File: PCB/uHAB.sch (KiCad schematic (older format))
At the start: 0 parts

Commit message: Finished power system design, added some custom schematic symbols, updated component selection document
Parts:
- added C? (x5): 47uF, symbol C
- added C?: 0.1uF, symbol C
- added D?: LED, symbol LED
- added F?: 0ZCJ0025AF2E, symbol Polyfuse
- added J?: Programming, symbol USB_OTG
- added J?: Battery_Input (5.6V-18V), symbol Conn_01x02
- added J?: Remove_Before_Flight_(RBF), symbol Conn_01x02
- added J?: Helmet_RBF_Jumper, symbol Conn_01x03
- added Q? (x3): SSM3J358R,LF, symbol Q_PMOS_GSD
- added Q?: NTR4003NTD, symbol Q_NMOS_GSD
- added R? (x2): 100k, symbol R
- added R?: R, symbol R
- added R? (x3): 10k, symbol R
- added R? (x2): 22, symbol R
- added U?: LDL1117S50R, TO_SOT_Packages_SMD:SOT-223-3Lead_TabPin2, symbol AP1117-15
- added U?: LDL1117S33R, TO_SOT_Packages_SMD:SOT-223-3Lead_TabPin2, symbol AP1117-15
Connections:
- new net: F?.2, J?.1 (VBUS)
- new net: J?.2 (D-), R?.2
- new net: J?.3 (D+), R?.2
- new net: J?.2 (Pin_2), Q?.3 (D)
- new net: C?.1, Q?.2 (S), Q?.2 (S), R?.1
- new net: Q?.1 (G), R?.1
- new net: D?.2 (A), R?.1
- new net: D?.1 (K), Q?.3 (D)
- new net: Q?.1 (G), R?.1, R?.1
- new net: J?.1 (Pin_1), Q?.1 (G), R?.2
- new net +3.3V: C?.1, Q?.1 (G), R?.2, U?.2 (VO)
- new net +5V: C?.1, C?.1, Q?.3 (D), R?.2, U?.2 (VO), U?.3 (VI)
- new net GND: C?.2, C?.2, C?.2, C?.2, C?.2, C?.2, J?.1 (Pin_1), J?.3 (Pin_3), J?.5 (GND), J?.6 (Shield), Q?.2 (S), R?.1, R?.2, R?.2, U?.1 (GND), U?.1 (GND)
- new net HELMET_RBF: J?.1 (Pin_1)
- new net MAIN_POWER: C?.1, Q?.3 (D), R?.2, U?.3 (VI)
- new net UHAB_RBF: J?.2 (Pin_2), J?.2 (Pin_2)
- new net USB_D+: R?.1
- new net USB_D-: R?.1
- new net USB_POWER: C?.1, F?.1, Q?.2 (S)
- no-connect marks 0 -> 1
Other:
- note added: "Connector PN: \n5-103635-1\n\nMate PN: \n104257-1\n\nTerminal PN: \n1-104480-7\n----------"
- note added: "Connector PN: \nDF22R-2P-7.92DS(05)\n\nMate PN: \nDF22R-2S-7.92C(28)\n\nTerminal PN: \nDF22-1416SCF"
- note added: "Connector PN: \nUJ2-MIBH-4-SMT-TR"
- note added: "Header PN: \nM20-9990346\n\nJumper PN:\nSTC02SYAN"
- note added: "If main power is present, the USB power will\nbe blocked. If main power is not present, the\nUSB power will supply the 5V (and 3.3V) rail."
- note added: "Linear Regulators"
- note added: "Note: Both 5V and 3.3V must be present to \nilluminate the power good indication LED"
- note added: "Power Status Indication LED"
- note added: "Recommended:\n-2S LiPo Battery Pack\n-2S 18650 Battery Pack\n-9V Battery\n----------------"
- note added: "Remove Before Flight"
- note added: "Reverse\nPolarity\nProtection"
- note added: "USB Power Behavior"

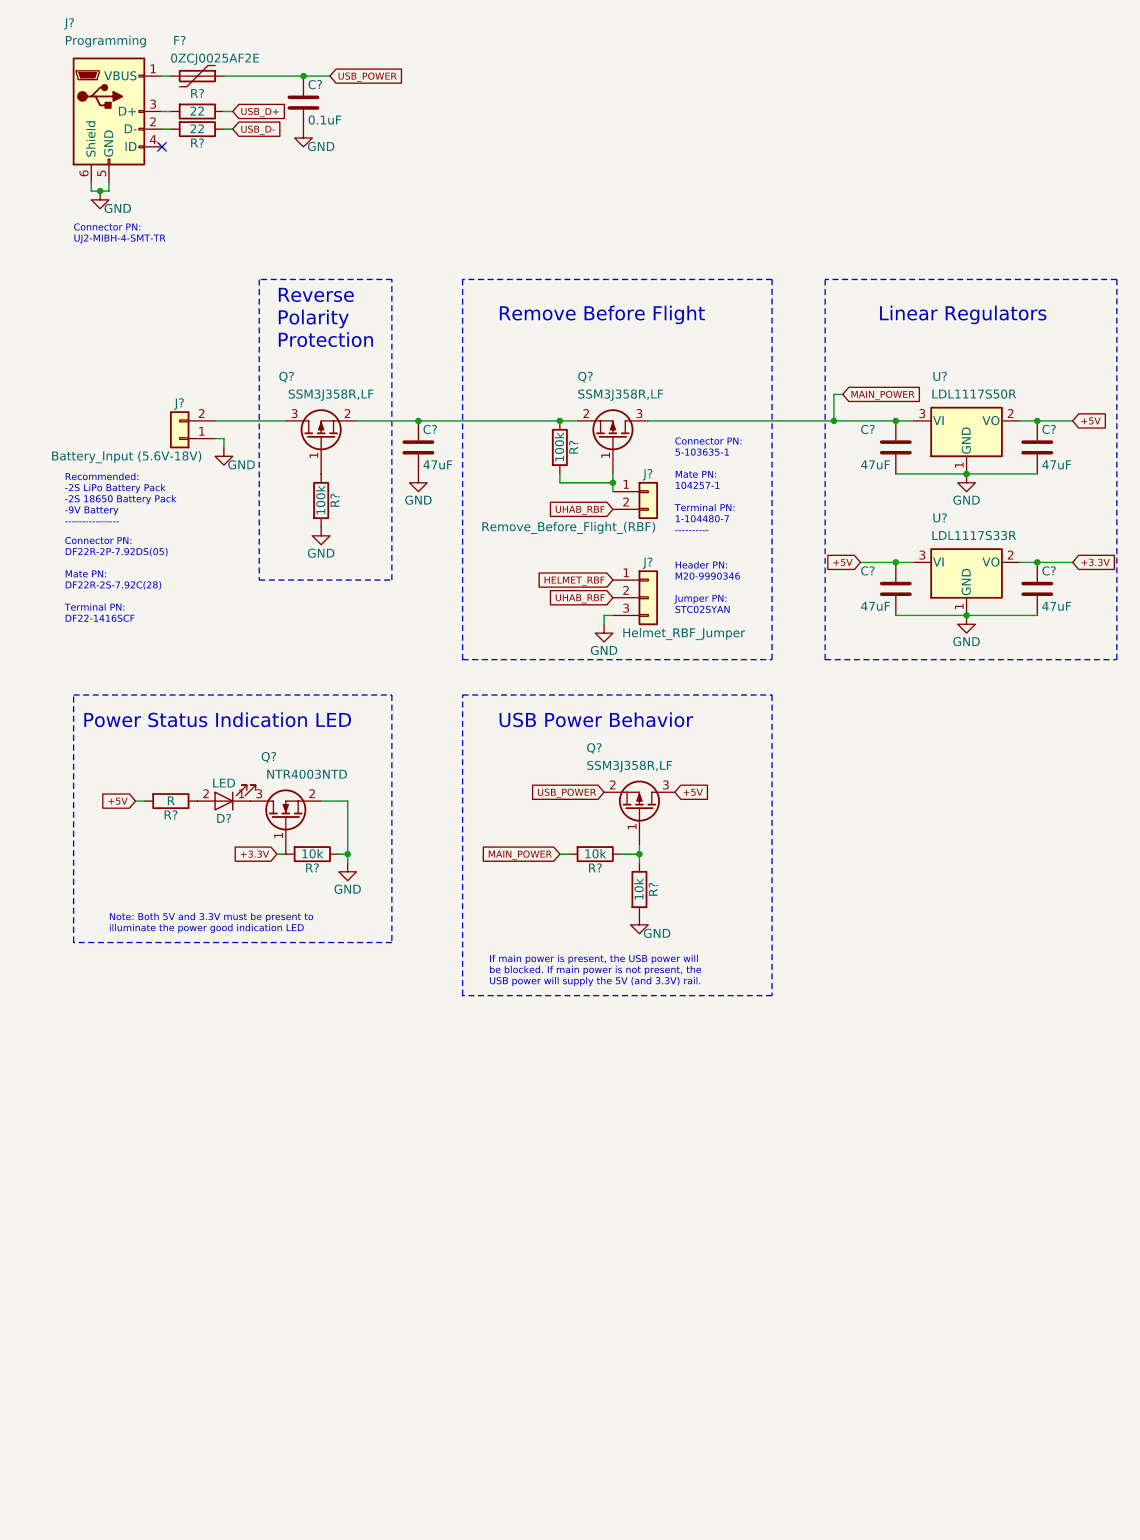
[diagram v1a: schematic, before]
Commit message: Added GPS Schematic, GPS datasheet, GPS user guide
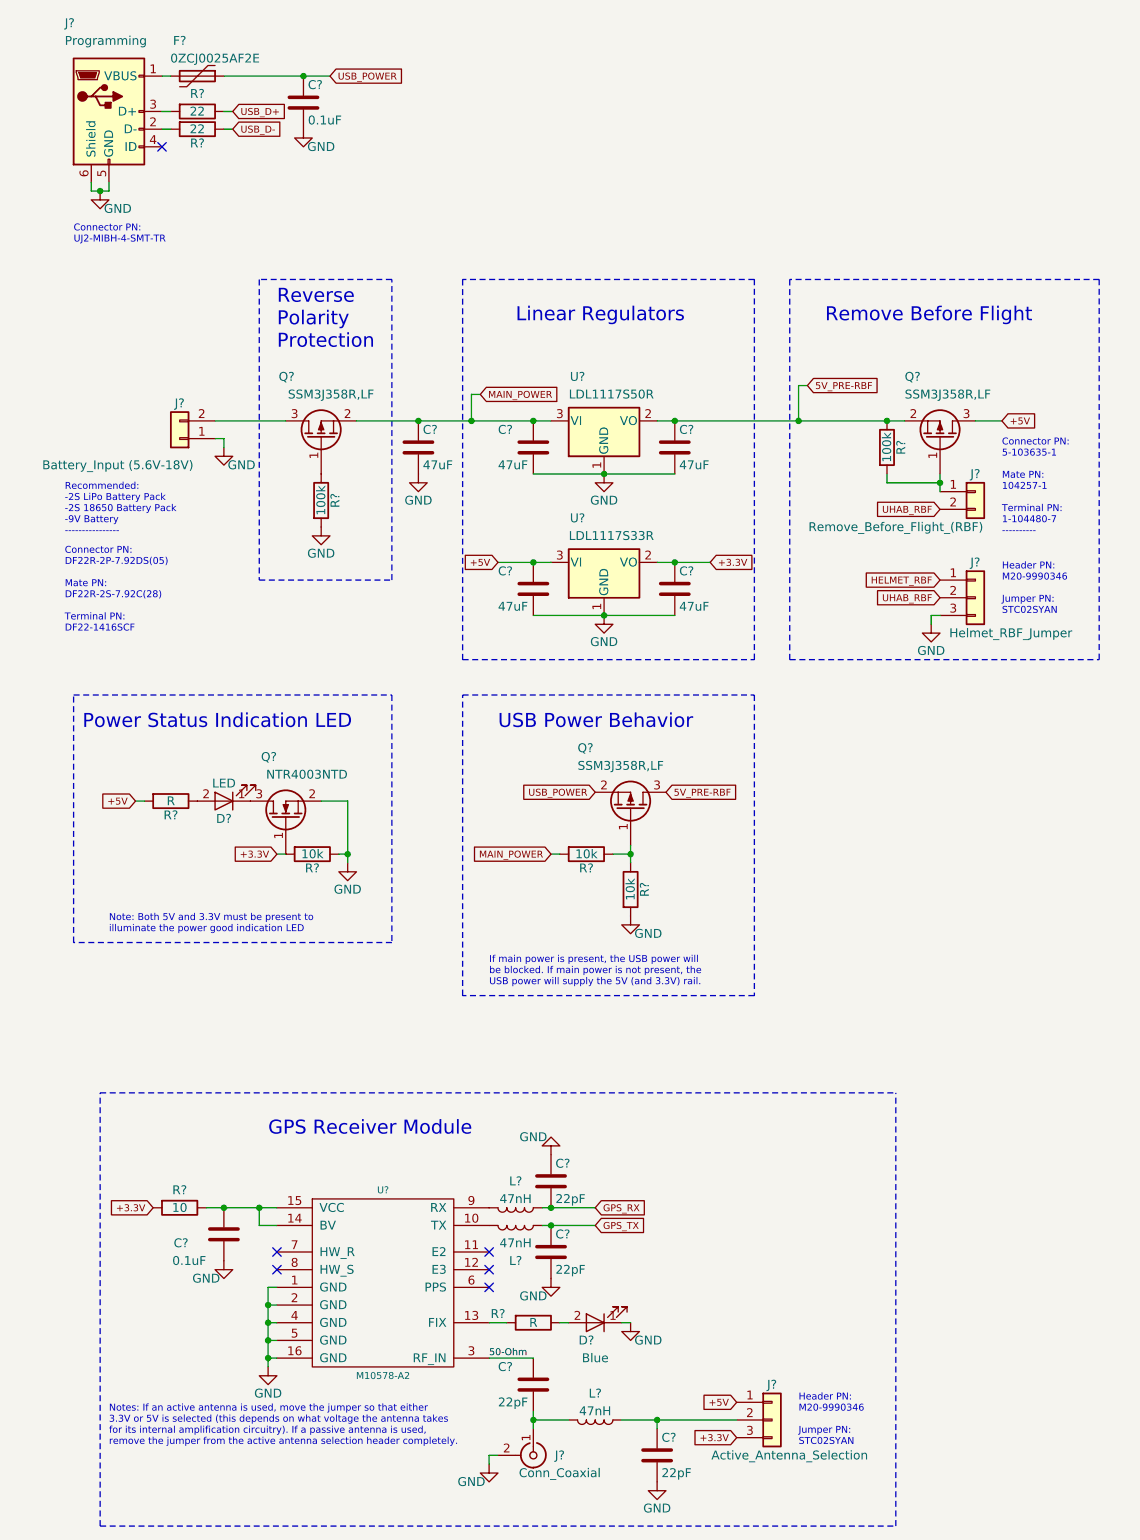
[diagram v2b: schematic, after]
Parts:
- added C?: 0.1uF, symbol C
- added C? (x4): 22pF, symbol C
- added D?: Blue, symbol LED
- added J?: Conn_Coaxial, symbol Conn_Coaxial
- added J?: Active_Antenna_Selection, symbol Conn_01x03
- added L? (x3): 47nH, symbol L
- added R?: 10, symbol R
- added R?: R, symbol R
- added U?: M10578-A2, symbol M10578-A2
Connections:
- net +3.3V: now also J?.3 (Pin_3), R?.2
- net +5V: now also Q?.3 (D), J?.1 (Pin_1); no longer C?.1, Q?.3 (D), U?.2 (VO)
- net GND: now also C?.1, C?.1, C?.2, C?.2, D?.1 (K), J?.2 (Ext), U?.1 (GND), U?.16 (GND), U?.2 (GND), U?.4 (GND), U?.5 (GND)
- net MAIN_POWER: now also C?.1, Q?.2 (S); no longer Q?.3 (D)
- net 5V_PRE-RBF: now reaches Q?.2 (S), R?.1
- net 5V_PRE-RBF: now also C?.1, Q?.3 (D), U?.2 (VO); no longer C?.1, Q?.2 (S)
- new net: L?.2, U?.10 (TX)
- new net: R?.2, U?.13 (FIX)
- new net: C?.2, R?.1, U?.14 (BV), U?.15 (VCC)
- new net: L?.2, U?.9 (RX)
- new net: D?.2 (A), R?.1
- new net: C?.2, J?.1 (In), L?.2
- new net: C?.1, J?.2 (Pin_2), L?.1
- new net 50-Ohm: C?.1, U?.3 (RF_IN)
- new net GPS_RX: C?.2, L?.1
- new net GPS_TX: C?.1, L?.1
- no-connect marks 1 -> 6
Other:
- note added: "GPS Receiver Module\n"
- note added: "Notes: If an active antenna is used, move the jumper so that either \n3.3V or 5V is selected (this depends on what voltage the antenna takes \nfor its internal amplification circuitry). If a passive antenna is used,\nremove the jumper from the active antenna selection header completely."
- moved on the sheet: C?, J?, Q?, R?, U?

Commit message: Added a ton to the schematic and included some additional documentation. Saving progress.
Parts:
- added C?: .01uF, symbol C
- added C?: 0.1uF, symbol C
- added C? (x16): 100nF, symbol C
- added C?: 10pF, symbol C
- added C? (x2): 10uF, symbol C
- added C? (x2): 12pF, symbol C
- added C?: 10nF, symbol C
- added C? (x2): 4.7pF, symbol C
- added D? (x3): LTST-C190KRKT, symbol LED
- added D?: 6.2V, symbol D_Zener
- added D?: LTST-C194KGKT, symbol LED
- added D?: LTST-C191TBKT, symbol LED
- added J?: Conn_Coaxial, symbol Conn_Coaxial
- added J?: Balloon_Cutdown, symbol Conn_01x02
- added J?: JTAG, symbol Conn_02x05_Odd_Even
- added L? (x3): BLM18PG471SN1, symbol L
- added Q?: SSM3J358R,LF, symbol Q_PMOS_GSD
- added Q? (x5): NTR4003NT1G, symbol Q_NMOS_GSD
- added Q?: IRLML62444, symbol Q_NMOS_GSD
- added R?: 0, symbol R
- added R? (x11): 100k, symbol R
- added R?: 680, symbol R
- added R?: 130, symbol R
- added R? (x2): 300, symbol R
- added R?: 170, symbol R
- added R? (x2): 10, symbol R
- added R?: 5.6k, symbol R
- added SW?: SW_Push, symbol SW_Push
- added U?: Radiometrix_HX1, symbol Radiometrix_HX1
- added U?: AT25DN256, symbol AT25DN256
- added U?: BLM18PG471SN1, MODULE, symbol ATSAMV71Q20B-AABT
- added Y?: 12MHz, symbol Crystal
- added Y?: 32.768kHz, symbol Crystal
- C?: value 0.1uF -> 47uF
- D?: value LED -> LTST-C194KGKT
- D?: value Blue -> LTST-C191TBKT
- Q?: value NTR4003NTD -> NTR4003NT1G
- R?: value R -> 300
- R? (x3): value 10k -> 100k
- R?: value R -> 170
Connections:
- net labels added: APRS_TX_5, BLUE_LED, CUTDOWN_ARM, CUTDOWN_FIRE, GREEN_LED, JTAGSEL, MEM_CS, MEM_MISO, MEM_MOSI, MEM_SCLK, PA00, PA01, PA02, PA03, PA04, PA05, PA06, PA09, PA10, PA11, PA12, PA13, PA14, PA15, PA16, PA17, PA18, PA19, PA20, PA21, PA22, PA23, PA24, PA25, PA26, PA27, PA28, PA29, PA30, PA31, PB00, PB01, PB02, PB03, PB04, PB05,TRACESWO, PB06,SWDIO, PB07,SWCLK, PB12, PB13, PC00, PC01, PC02, PC03, PC04, PC05, PC06, PC07, PC08, PC09, PC10, PC11, PC12, PC13, PC14, PC15, PC16, PC17, PC18, PC19, PC20, PC21, PC22, PC23, PC24, PC25, PC26, PC27, PC28, PC29, PC30, PC31, PD00, PD01, PD02, PD03, PD04, PD05, PD06, PD07, PD08, PD09, PD10, PD11, PD12, PD13, PD14, PD15, PD16, PD17, PD18, PD19, PD20, PD21, PD22, PD23, PD24, PD25, PD26, PD27, PD28, PD29, PD30, PD31, PE00, PE01, PE02, PE03, PE04, PE05, RED_LED, TARGET_RESET, TST, VDDCORE, VDDPLL, VDDUTMIC, XIN, XIN_32, XOUT, XOUT_32
- wire segments 57 -> 227
- no-connect marks 6 -> 10
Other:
- note added: "12MHz Crystal"
- note added: "256Kb Flash Memory"
- note added: "32.768kHz Crystal"
- note added: "APRS Transmit Radio"
- note added: "Balloon Cutdown"
- note added: "C_Crystal = 20pF\nmax ESR = 80 Ohm\nAccuracy = 20ppm"
- note added: "C_Crystal = 7pF\nmax ESR = 60 kOhm\nAccuracy = 20ppm"
- note added: "Controllable LEDs"
- note added: "Design Note: 10mA for this LED"
- note added: "External & Internal Power Decoupling"
- note added: "JTAG Programming Connector"
- note added: "Reset Pushbutton"
- note added: "USB Micro Power & Programming"
- moved on the sheet: C?, D?, F?, J?, L?, Q?, R?, U?

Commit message: Updated Schematic. Documentation still needs a lot of work
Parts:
- removed C?: .01uF, symbol C
- removed J?: Conn_Coaxial, symbol Conn_Coaxial
- removed R?: 0, symbol R
- removed U?: Radiometrix_HX1, symbol Radiometrix_HX1
- added .01uF: C, symbol C
- added C?: 100pF, symbol C
- added C?: 6.2pF, symbol C
- added C?: 12pF, symbol C
- added C? (x5): 560pF, symbol C
- added C?: 3.3pF, symbol C
- added C?: 22pF, symbol C
- added C?: 15pF, symbol C
- added C? (x2): 20pF, symbol C
- added C? (x3): 0.1uF, symbol C
- added D?: Green, symbol LED
- added D?: Red, symbol LED
- added L?: 200nH, symbol L
- added L?: 150nH, symbol L
- added L?: 470nH, symbol L
- added L?: 56nH, symbol L
- added L?: 82nH, symbol L
- added L?: 100nH, symbol L
- added L?: 560nH, symbol L
- added L?: 110nH, symbol L
- added P?: SMA, symbol Coax_connector
- added R? (x2): 10, symbol R
- added R?: 100k, symbol R
- added R? (x2): R, symbol R
- added R?: 0, symbol R
- added U?: Si4464-B1B-FM, symbol Si4464-B1B-FM
- added U?: S179-92LF, symbol AS2133-92LF
- added U?: DSC6101CI2A-026, symbol KT2016K26000BCW18ZAS
- added U?: MAAP-011232-TR0500, symbol MAAP-011232-TR0500
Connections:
- net labels added: +9V, AMP_CTL, OSC_26MHz, RADIO_CS, RADIO_GPIO0, RADIO_GPIO1, RADIO_IRQ, RADIO_MISO, RADIO_MOSI, RADIO_RX, RADIO_SCK, RADIO_SDN, RADIO_TX, RX_CTL, TX_CTL
- net labels removed: APRS_TX_5
- wire segments 227 -> 294
- no-connect marks 10 -> 21
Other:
- note added: "26MHz Oscillator"
- note added: "50 Ohm"
- note added: "APRS Transciever"
- note added: "Amplifier"
- note added: "Antenna Connection"
- note added: "Cortex M-7 Microcontroller"
- note added: "RF Switch"
- note removed: "APRS Transmit Radio"
- moved on the sheet: C?, J?, L?, R?, U?, Y?

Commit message: Removing file that is too large
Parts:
- added C? (x2): 20pF, symbol C
- added C?: 1uF, symbol C
- added C? (x3): 47uF, symbol C
- added C? (x2): 0.1uF, symbol C
- added C?: 100pF, symbol C
- added C?: 10pF, symbol C
- added C?: 680pF, symbol C
- added C?: 47pF, symbol C
- added L?: 100nH, symbol L
- added L?: XPL7030-472ML, symbol L
- added L?: LXPL7030-472ML, symbol L
- added R? (x2): 100k, symbol R
- added R?: 42.2k, symbol R
- added R?: 33k, symbol R
- added R?: 28k, symbol R
- added R?: 287k, symbol R
- added R?: 69.8k, symbol R
- added R?: 1.15M, symbol R
- added R?: 10k, symbol R
- added U?: LTC3112, symbol LTC3112
- J?: value Battery_Input (5.6V-18V) -> Battery_Input (3V-15V)
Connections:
- net +9V: now also C?.1, R?.2, U?.3 (VI), C?.1, L?.2
- net GND: now also C?.2, C?.2, C?.2, C?.2, C?.2, C?.2, C?.2, R?.1, R?.2, R?.2, U?.17 (GND)
- net at U?.1 (IN1): now also C?.1, L?.1; no longer C?.1
- net MAIN_POWER renamed Battery_PWR
- net Battery_PWR: now also C?.1, R?.1, U?.5 (VIN); no longer C?.1, R?.2, U?.3 (VI)
- new net: C?.1, C?.1, L?.2
- new net: C?.2, R?.2, U?.1 (COMP)
- new net: C?.2, U?.11 (BST2)
- new net: C?.1, L?.1, U?.13 (SW1)
- new net: C?.2, U?.14 (BST1)
- new net: C?.1, R?.1, U?.15 (VCC)
- new net: R?.2, U?.16 (PWM)
- new net: C?.1, C?.1, R?.1, R?.2, R?.2, U?.2 (FB)
- new net: R?.2, R?.2, U?.3 (OVP)
- new net: R?.2, U?.6 (RUN)
- new net: C?.1, R?.1, U?.7 (IOUT)
- new net: C?.1, C?.1, L?.1, R?.1, R?.1, U?.8 (VOUT)
- new net: C?.1, L?.2, U?.9 (SW2)
- new net: C?.2, R?.1 (x2)
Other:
- note added: "9V, 2.5A Buck/Boost \nSwitching Regulator"
- note added: "If 9V power rail is present, the USB power will\nbe blocked. If main power is not present, the\nUSB power will supply the 5V (and 3.3V) rail."
- note added: "TODO: Move RBF to Before Linear Regulators\n*Karlie Agrees*"
- note removed: "If main power is present, the USB power will\nbe blocked. If main power is not present, the\nUSB power will supply the 5V (and 3.3V) rail."
- moved on the sheet: C?, D?, J?, L?, P?, Q?, R?, SW?, U?, Y?

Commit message: Push of multiple things...havent pushed in a while. Continuing development on another PC
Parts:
- added C? (x5): 1uF, symbol C
- added C?: 10uF, symbol C
- added R? (x4): 10, symbol R
- added R? (x2): 10k, symbol R
- added U?: MCP4706, symbol MCP4706
- added U?: AD8541, symbol MCP6001
- added U?: LM2776, symbol LM2776
- C? (x5): value 0.1uF -> 1uF
- C?: renamed from .01uF; value C -> 1uF
- D? (x9): symbol LED -> LED-RESCUE-uHAB
- J?: symbol USB_OTG -> USB_OTG-RESCUE-uHAB
- J?: value Battery_Input (3V-15V) -> Battery_Input (5V-15V)
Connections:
- net +5V: now also R?.2, R?.2, R?.2
- net GND: now also C?.2, C?.2, C?.2, C?.2, C?.2, U?.2 (GND), U?.2 (VSS), U?.3 (+)
- net AMP_CTL renamed PWR_AMP_CTL_NEG
- net PWR_AMP_CTL_NEG: now also R?.1, U?.1
- new net: C?.1, R?.1, U?.3 (VDD)
- new net: R?.1, R?.2, U?.4 (-)
- new net: C?.1, R?.1, U?.5 (V+)
- new net: C?.1, R?.1, U?.3 (VDD), U?.4 (EN)
- new net: C?.1, U?.5 (C1+)
- new net: C?.2, U?.6 (C1-)
- new net -5V: C?.1, R?.2, U?.1 (VOUT)
- new net NEG_PWR: C?.1, R?.1, U?.2 (V-)
- new net PWR_AMP_CTL_POS: R?.2, U?.1 (VOUT)
- new net UHAB_SCL: U?.5 (SCL)
- new net UHAB_SDA: U?.4 (SDA)
- no-connect marks 21 -> 22
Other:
- note added: "Amplifier Control DAC"
- note added: "Amplifier Control \nVoltage Inverter"
- note added: "I2C Address: 0x60"
- note added: "Negative 5V Generation \nfor Operational Amplifier(s)"
- note removed: "TODO: Move RBF to Before Linear Regulators\n*Karlie Agrees*"
- moved on the sheet: C?, Y?
